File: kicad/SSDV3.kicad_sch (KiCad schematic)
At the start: 72 parts, among them J1 SolderPad, J2 SolderPad, J3 SolderPad, J4 SolderPad, J5 SolderPad, J6 SolderPad, J7 SolderPad_01x02, J8 SolderPad_1x03, Q1 CSD19537Q3, Q2 CSD19537Q3, Q3 BSZ096N10LS5, U1 LM5050-1, U2 LM5146RGYR

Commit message: Officially now the SSDV3
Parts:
- U2: footprint LM5146RGYR:RGY0020B-MFG -> ul_LM5146RGYR:RGY0020B-MFG-ThermalVias
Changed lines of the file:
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@@
 	(title_block
 		(title "Super Step Down V3")
-		(date "2025-10-19")
+		(date "2025-10-20")
 		(rev "C")
 		(company "UBCO Aerospace [Julian Joaquin]")
@@
 			)
 		)
-		(property "Footprint" "LM5146RGYR:RGY0020B-MFG"
+		(property "Footprint" "ul_LM5146RGYR:RGY0020B-MFG-ThermalVias"
 			(at 101.6 124.46 0)
 			(effects

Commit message: Minor layout improvements, using original footprints
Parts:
- U2: footprint ul_LM5146RGYR:RGY0020B-MFG-ThermalVias -> Package_QFN_JJ:Texas_RGY0020B_EP_3.5x4.5mm_P0.5mm_ThermalVias-D0.3mm
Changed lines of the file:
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@@
 			)
 		)
-		(property "Footprint" "ul_LM5146RGYR:RGY0020B-MFG-ThermalVias"
+		(property "Footprint" "Package_QFN_JJ:Texas_RGY0020B_EP_3.5x4.5mm_P0.5mm_ThermalVias-D0.3mm"
 			(at 101.6 124.46 0)
 			(effects

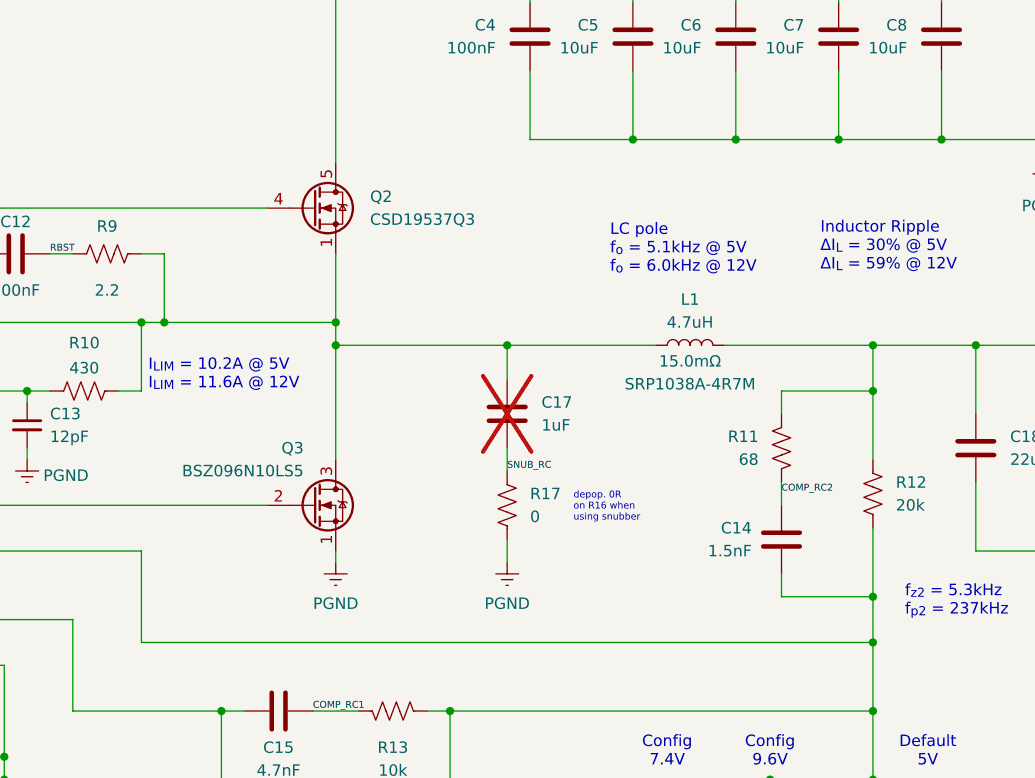
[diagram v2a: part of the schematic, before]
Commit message: Added schematic details, added license, improved README
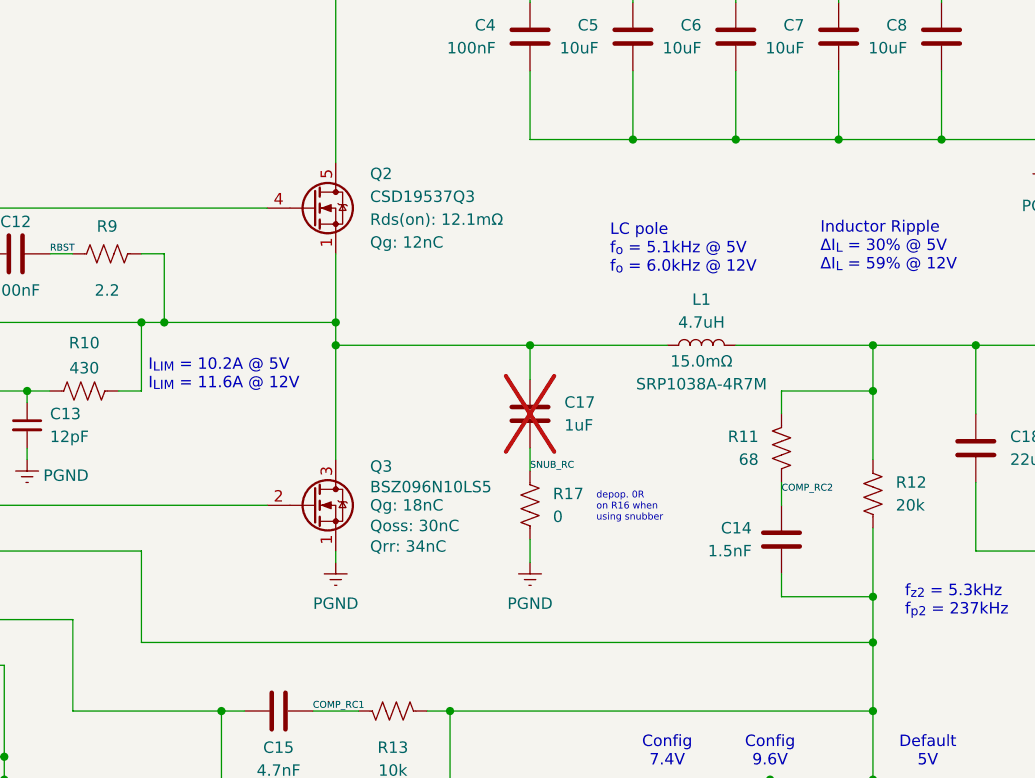
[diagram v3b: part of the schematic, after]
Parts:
- Q2: ESR 12.1mΩ -> (none); Qg (none) -> 12nC; Rds(on) (none) -> 12.1mΩ
- Q3: Qg (none) -> 18nC; Qoss (none) -> 30nC; Qrr (none) -> 34nC
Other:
- company: UBCO Aerospace [Julian Joaquin] -> Julian Joaquin
- moved on the sheet: C17, L1, R17

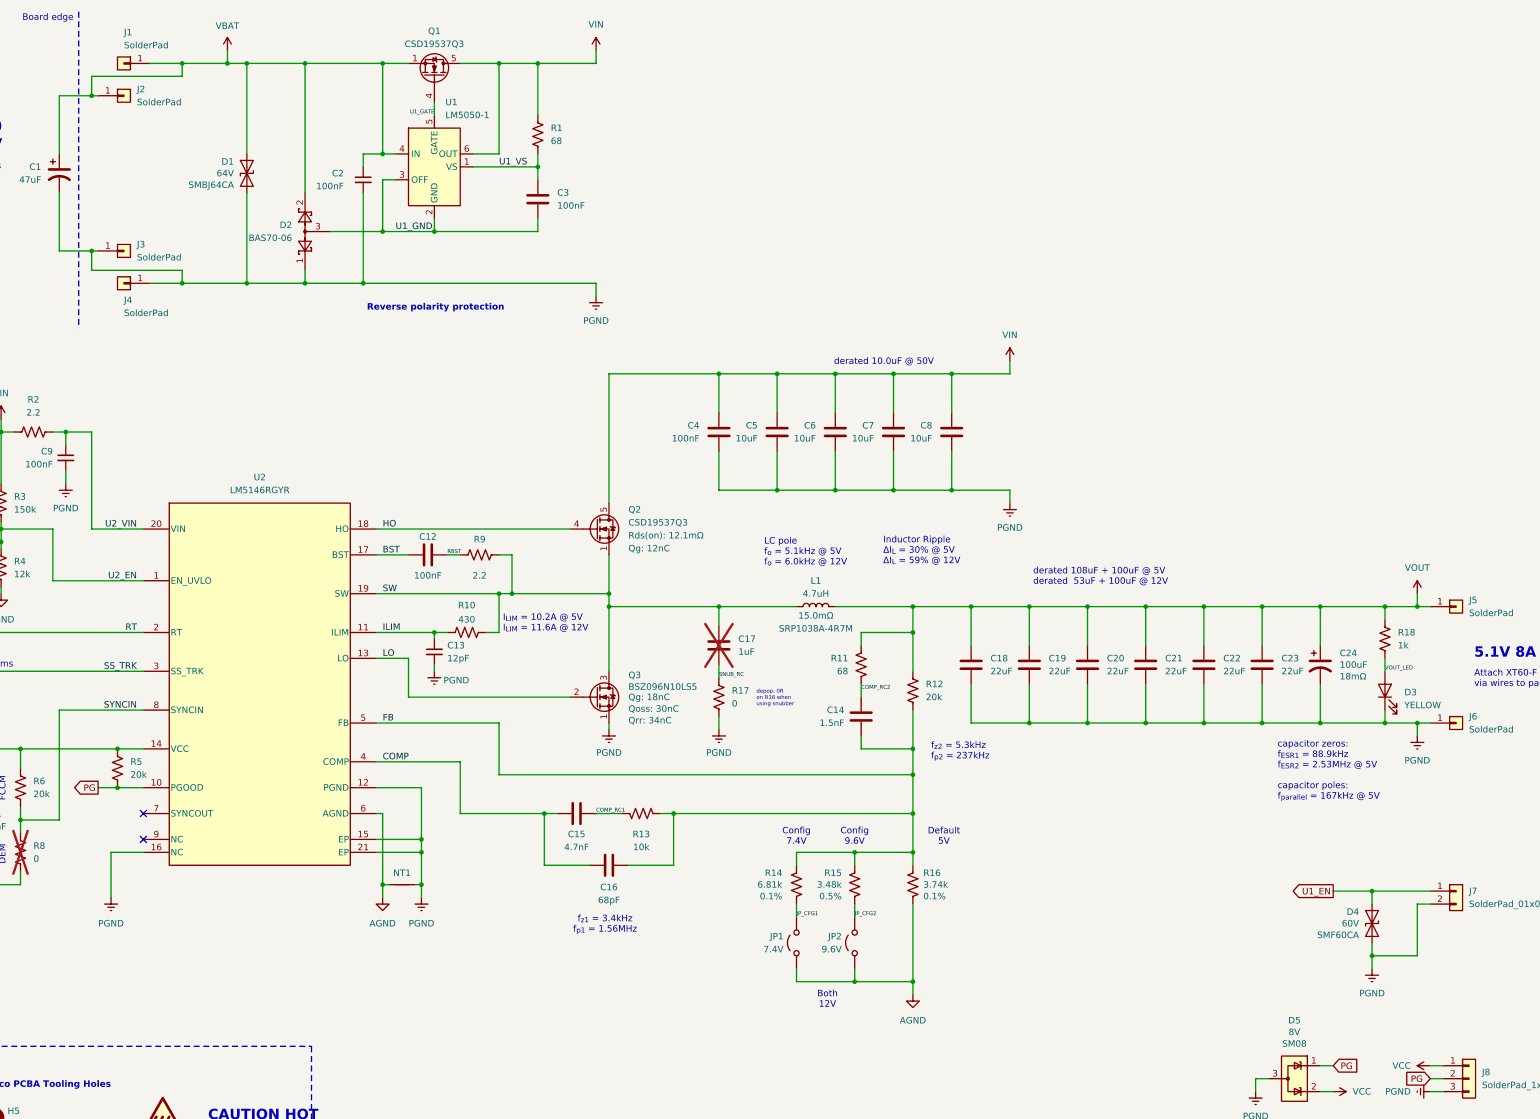
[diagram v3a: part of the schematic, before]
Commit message: revD started, fixed reverse polarity issues and improve temp rating
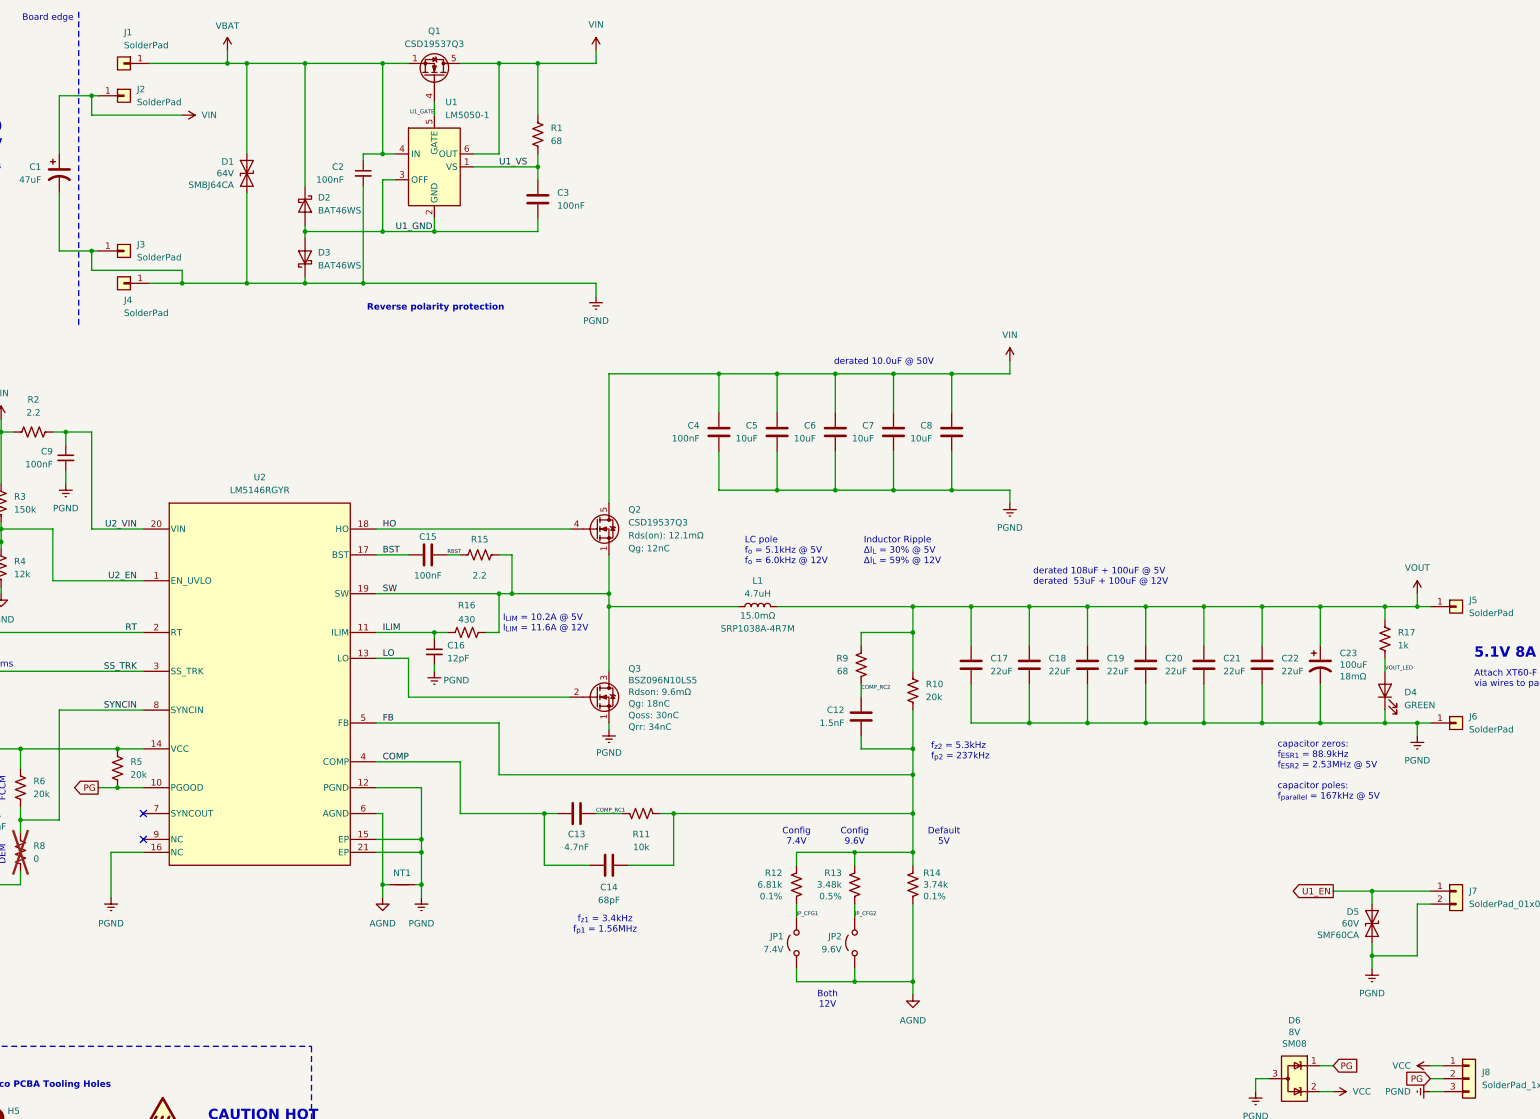
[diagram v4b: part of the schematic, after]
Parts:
- removed C17: 1uF, Capacitor_SMD:C_0603_1608Metric_Pad1.08x0.95mm_HandSolder, symbol Device:C
- removed D2: BAS70-06, Package_TO_SOT_SMD:SOT-23-3, symbol Diode:BAT54AW
- removed R17: 0, Resistor_SMD:R_1206_3216Metric_Pad1.30x1.75mm_HandSolder, symbol Device:R_US
- added D2, D3: BAT46WS, Diode_SMD:D_SOD-323, symbol Device:D_Schottky
- C10: LCSC PN C377773 -> C77081; Manufacturer Panasonic -> Murata Electronics; Part Number CL21A225KBQNNNE -> GRM21BR71E225KE11L; Part Type Basic -> Extended; Voltage 50V -> 25V
- C17: renamed from C18; LCSC PN C52306 -> C309062; Part Number CL32A226KAJNNNE -> CL32B226KAJNNNE
- C18: renamed from C19; LCSC PN C52306 -> C309062; Part Number CL32A226KAJNNNE -> CL32B226KAJNNNE
- C19: renamed from C20; LCSC PN C52306 -> C309062; Part Number CL32A226KAJNNNE -> CL32B226KAJNNNE
- C20: renamed from C21; LCSC PN C52306 -> C309062; Part Number CL32A226KAJNNNE -> CL32B226KAJNNNE
- C21: renamed from C22; LCSC PN C52306 -> C309062; Part Number CL32A226KAJNNNE -> CL32B226KAJNNNE
- C22: renamed from C23; LCSC PN C52306 -> C309062; Part Number CL32A226KAJNNNE -> CL32B226KAJNNNE
- D4: renamed from D3; value YELLOW -> GREEN; LCSC PN C2296 -> C2297; Part Number KT-0805Y -> KT-0805G
- Q3: Rdson (none) -> 9.6mΩ
- renumbered C14 to C12, C15 to C13, C16 to C14, C12 to C15, C13 to C16, C24 to C23, D4 to D5, D5 to D6, R12 to R10, R13 to R11, R14 to R12, R15 to R13, R16 to R14, R9 to R15, R10 to R16, R18 to R17, R11 to R9
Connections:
- net PGND: now also D3.1 (K)
- net U1_GND: now also D2.2 (A), D3.2 (A)
- net VBAT: now also D2.1 (K); no longer C1.1, J2.1 (Pin_1)
- net VIN: now also C1.1, J2.1 (Pin_1)
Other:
- note removed: "depop. 0R on R16 when using snubber"
- moved on the sheet: C2, L1
